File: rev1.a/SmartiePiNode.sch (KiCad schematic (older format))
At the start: 57 parts, among them CN1 USBMICROb, CN2 SWD, CN3 SX1238_TRX_HEADER, CN4 VIN, SW1 SW_PUSH, U1 ISL91127IR, U2 STM32L052_LQFP48, X1 abm10, X2 ABS25-32.768KHZ-6-T

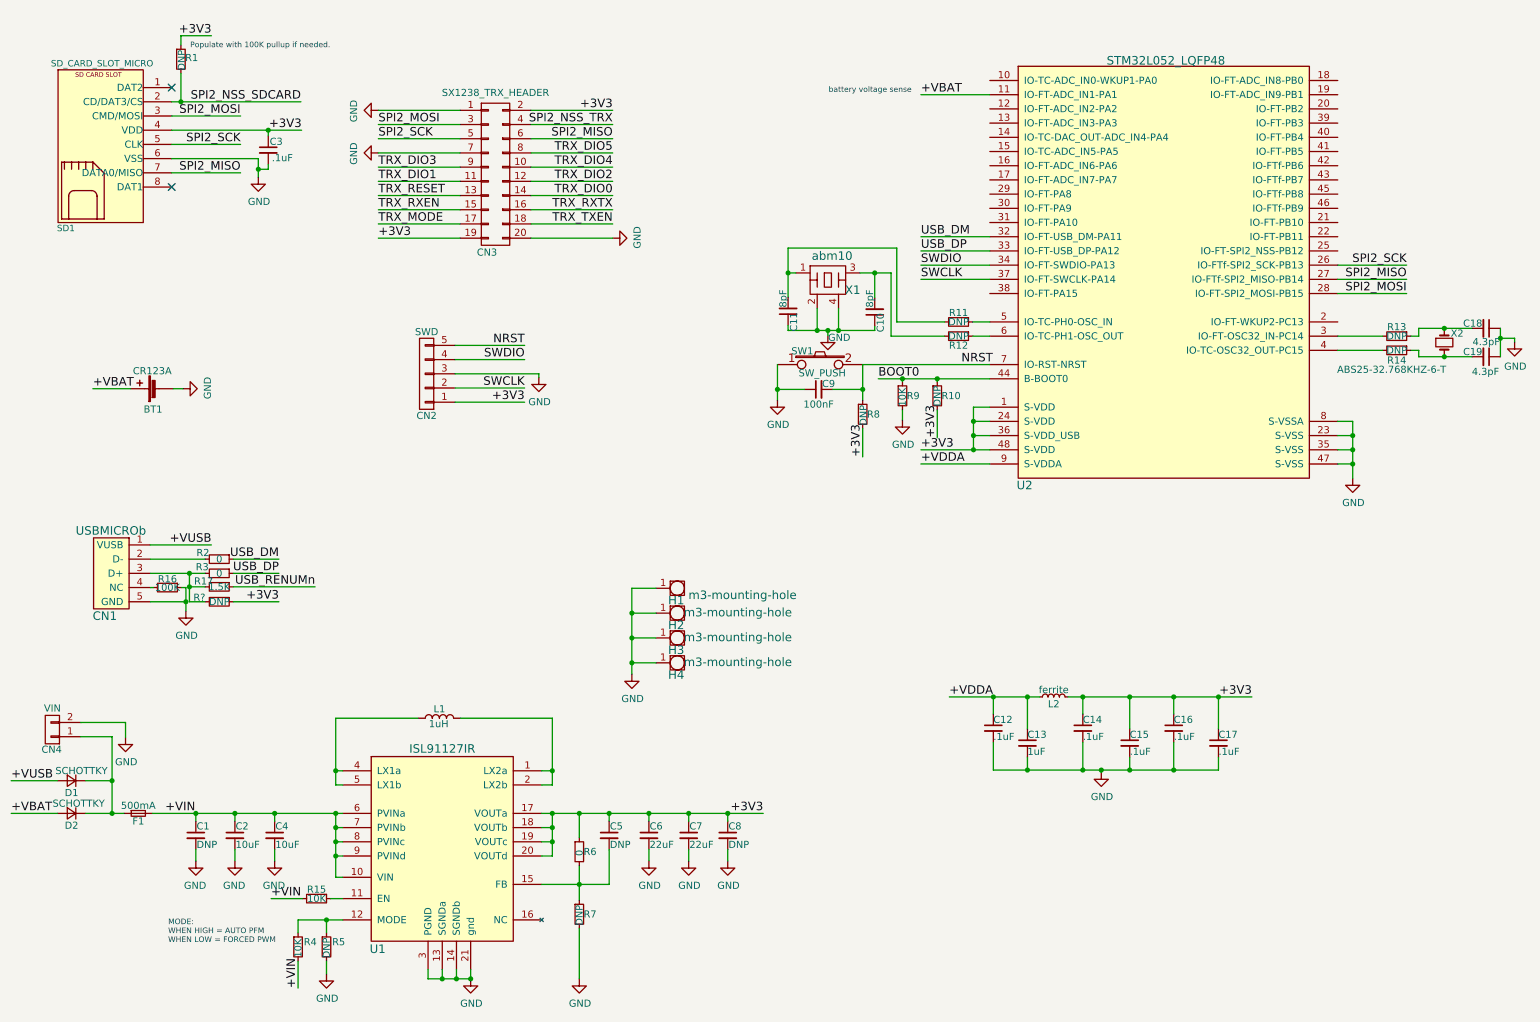
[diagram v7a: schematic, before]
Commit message: added battery sensing circuit and a bit more work on usb.
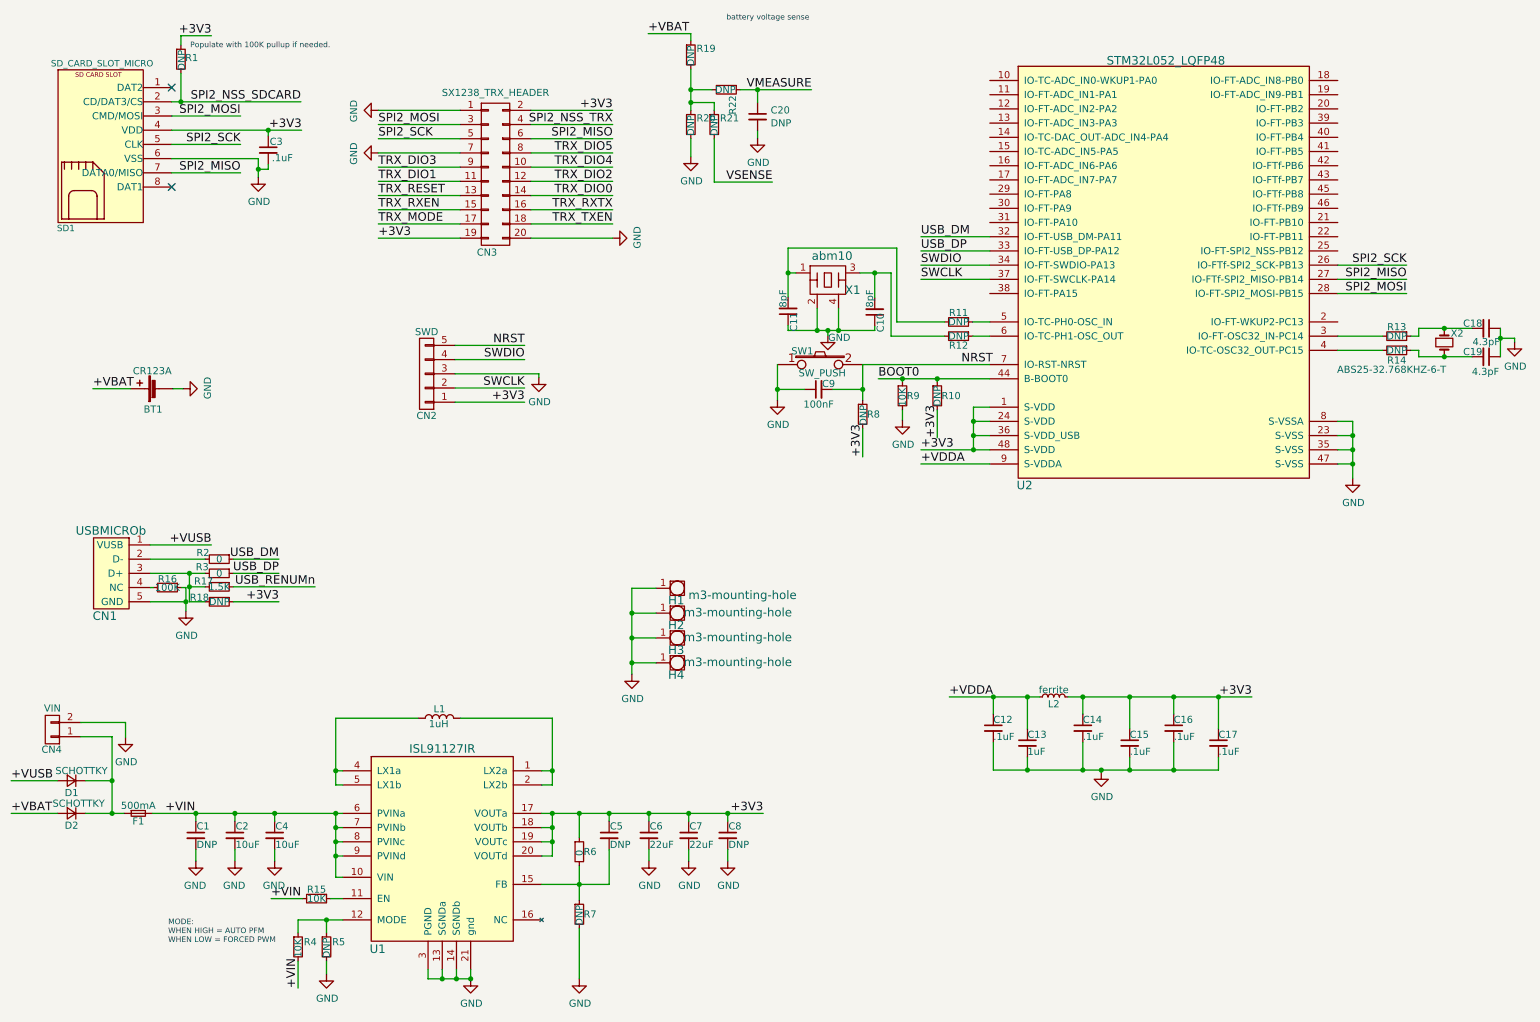
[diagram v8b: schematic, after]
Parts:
- added C20: DNP, Capacitors_SMD:C_0603, symbol C_Small
- added R19, R20, R21, R22: DNP, Resistors_SMD:R_0603, symbol R_Small
- R18: renamed from R?; footprint (none) -> Resistors_SMD:R_0603
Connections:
- net +VBAT: now also R19.1; no longer U2.11 (IO-FT-ADC_IN1-PA1)
- net GND: now also C20.2, R20.2
- new net: R19.2, R20.1, R21.1, R22.2
- new net VMEASURE: C20.1, R22.1
- new net VSENSE: R21.2
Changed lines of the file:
@@
 $EndComp
 $Comp
-L GND #PWR01
+L GND #PWR11
 U 1 1 5B041A53
 P 3720 7315
-F 0 "#PWR01" H 3720 7065 50  0001 C CNN
+F 0 "#PWR11" H 3720 7065 50  0001 C CNN
 F 1 "GND" H 3725 7142 50  0000 C CNN
 F 2 "" H 3720 7315 50  0001 C CNN
@@
 $EndComp
 $Comp
-L GND #PWR02
+L GND #PWR16
 U 1 1 5B041F18
 P 4975 6485
-F 0 "#PWR02" H 4975 6235 50  0001 C CNN
+F 0 "#PWR16" H 4975 6235 50  0001 C CNN
 F 1 "GND" H 4980 6312 50  0000 C CNN
 F 2 "" H 4975 6485 50  0001 C CNN
@@
 $EndComp
 $Comp
-L GND #PWR03
+L GND #PWR17
 U 1 1 5B04234F
 P 5255 6485
-F 0 "#PWR03" H 5255 6235 50  0001 C CNN
+F 0 "#PWR17" H 5255 6235 50  0001 C CNN
 F 1 "GND" H 5260 6312 50  0000 C CNN
 F 2 "" H 5255 6485 50  0001 C CNN
@@
 $EndComp
 $Comp
-L GND #PWR04
+L GND #PWR19
 U 1 1 5B0423C8
 P 5530 6485
-F 0 "#PWR04" H 5530 6235 50  0001 C CNN
+F 0 "#PWR19" H 5530 6235 50  0001 C CNN
 F 1 "GND" H 5535 6312 50  0000 C CNN
 F 2 "" H 5530 6485 50  0001 C CNN
@@
 $EndComp
 $Comp
-L GND #PWR05
+L GND #PWR7
 U 1 1 5B04306E
 P 2340 6485
-F 0 "#PWR05" H 2340 6235 50  0001 C CNN
+F 0 "#PWR7" H 2340 6235 50  0001 C CNN
 F 1 "GND" H 2345 6312 50  0000 C CNN
 F 2 "" H 2340 6485 50  0001 C CNN
@@
 $EndComp
 $Comp
-L GND #PWR06
+L GND #PWR5
 U 1 1 5B04307C
 P 2060 6485
-F 0 "#PWR06" H 2060 6235 50  0001 C CNN
+F 0 "#PWR5" H 2060 6235 50  0001 C CNN
 F 1 "GND" H 2065 6312 50  0000 C CNN
 F 2 "" H 2060 6485 50  0001 C CNN
@@
 $EndComp
 $Comp
-L GND #PWR07
+L GND #PWR4
 U 1 1 5B04308A
 P 1785 6485
-F 0 "#PWR07" H 1785 6235 50  0001 C CNN
+F 0 "#PWR4" H 1785 6235 50  0001 C CNN
 F 1 "GND" H 1790 6312 50  0000 C CNN
 F 2 "" H 1785 6485 50  0001 C CNN
@@
 $EndComp
 $Comp
-L GND #PWR08
+L GND #PWR8
 U 1 1 5B043F5D
 P 2705 7280
-F 0 "#PWR08" H 2705 7030 50  0001 C CNN
+F 0 "#PWR8" H 2705 7030 50  0001 C CNN
 F 1 "GND" H 2710 7107 50  0000 C CNN
 F 2 "" H 2705 7280 50  0001 C CNN
@@
 $EndComp
 $Comp
-L GND #PWR09
+L GND #PWR13
 U 1 1 5B044D4C
 P 4485 7315
-F 0 "#PWR09" H 4485 7065 50  0001 C CNN
+F 0 "#PWR13" H 4485 7065 50  0001 C CNN
 F 1 "GND" H 4490 7142 50  0000 C CNN
 F 2 "" H 4485 7315 50  0001 C CNN
@@
 $EndComp
 $Comp
-L GND #PWR010
+L GND #PWR25
 U 1 1 5B06F6EF
 P 9930 3790
-F 0 "#PWR010" H 9930 3540 50  0001 C CNN
+F 0 "#PWR25" H 9930 3540 50  0001 C CNN
 F 1 "GND" H 9935 3617 50  0000 C CNN
 F 2 "" H 9930 3790 50  0001 C CNN
@@
 $EndComp
 $Comp
-L GND #PWR011
+L GND #PWR23
 U 1 1 5B0753BB
 P 6760 3380
-F 0 "#PWR011" H 6760 3130 50  0001 C CNN
+F 0 "#PWR23" H 6760 3130 50  0001 C CNN
 F 1 "GND" H 6765 3207 50  0000 C CNN
 F 2 "" H 6760 3380 50  0001 C CNN
@@
 $EndComp
 $Comp
-L GND #PWR012
+L GND #PWR3
 U 1 1 5B081C3A
 P 1715 4725
-F 0 "#PWR012" H 1715 4475 50  0001 C CNN
+F 0 "#PWR3" H 1715 4475 50  0001 C CNN
 F 1 "GND" H 1720 4552 50  0000 C CNN
 F 2 "" H 1715 4725 50  0001 C CNN
@@
 $EndComp
 $Comp
-L GND #PWR013
+L GND #PWR21
 U 1 1 5B082DC4
 P 5880 3240
-F 0 "#PWR013" H 5880 2990 50  0001 C CNN
+F 0 "#PWR21" H 5880 2990 50  0001 C CNN
 F 1 "GND" H 5885 3067 50  0000 C CNN
 F 2 "" H 5880 3240 50  0001 C CNN
@@
 Connection ~ 10575 2935
 $Comp
-L GND #PWR014
+L GND #PWR26
 U 1 1 5B098D9A
 P 11070 2830
-F 0 "#PWR014" H 11070 2580 50  0001 C CNN
+F 0 "#PWR26" H 11070 2580 50  0001 C CNN
 F 1 "GND" H 11075 2657 50  0000 C CNN
 F 2 "" H 11070 2830 50  0001 C CNN
@@
 	2225 1540 2225 1670
 $Comp
-L GND #PWR015
+L GND #PWR6
 U 1 1 5B0A5E1E
 P 2225 1670
-F 0 "#PWR015" H 2225 1420 50  0001 C CNN
+F 0 "#PWR6" H 2225 1420 50  0001 C CNN
 F 1 "GND" H 2230 1497 50  0000 C CNN
 F 2 "" H 2225 1670 50  0001 C CNN
@@
 +3V3
 $Comp
-L GND #PWR016
+L GND #PWR9
 U 1 1 5B0AC996
 P 3070 1200
-F 0 "#PWR016" H 3070 950 50  0001 C CNN
+F 0 "#PWR9" H 3070 950 50  0001 C CNN
 F 1 "GND" H 3075 1027 50  0000 C CNN
 F 2 "" H 3070 1200 50  0001 C CNN
@@
 SPI2_SCK
 $Comp
-L GND #PWR017
+L GND #PWR10
 U 1 1 5B0AE690
 P 3070 1500
-F 0 "#PWR017" H 3070 1250 50  0001 C CNN
+F 0 "#PWR10" H 3070 1250 50  0001 C CNN
 F 1 "GND" H 3075 1327 50  0000 C CNN
 F 2 "" H 3070 1500 50  0001 C CNN
@@
 	4145 2100 4720 2100
 $Comp
-L GND #PWR018
+L GND #PWR14
 U 1 1 5B0AEB87
 P 4720 2100
-F 0 "#PWR018" H 4720 1850 50  0001 C CNN
+F 0 "#PWR14" H 4720 1850 50  0001 C CNN
 F 1 "GND" H 4725 1927 50  0000 C CNN
 F 2 "" H 4720 2100 50  0001 C CNN
@@
 	1625 3160 1695 3160
 $Comp
-L GND #PWR019
+L GND #PWR2
 U 1 1 5B0B10C1
 P 1695 3160
-F 0 "#PWR019" H 1695 2910 50  0001 C CNN
+F 0 "#PWR2" H 1695 2910 50  0001 C CNN
 F 1 "GND" H 1700 2987 50  0000 C CNN
 F 2 "" H 1695 3160 50  0001 C CNN
@@
 Wire Wire Line
 	810  5920 485  5920
-Wire Wire Line
-	6890 1090 7375 1090
-Text Label 6890 1090 0    60   ~ 0
+Text Label 4970 660  0    60   ~ 0
 +VBAT
-Text Notes 6240 1085 0    39   ~ 0
+Text Notes 5520 575  0    39   ~ 0
 battery voltage sense
 $Comp
@@
 NRST
 $Comp
-L GND #PWR020
+L GND #PWR12
 U 1 1 5B0B8F14
 P 4200 3080
-F 0 "#PWR020" H 4200 2830 50  0001 C CNN
+F 0 "#PWR12" H 4200 2830 50  0001 C CNN
 F 1 "GND" H 4205 2907 50  0000 C CNN
 F 2 "" H 4200 3080 50  0001 C CNN
@@
 $EndComp
 $Comp
-L GND #PWR021
+L GND #PWR24
 U 1 1 5B0C38AE
 P 8160 5860
-F 0 "#PWR021" H 8160 5610 50  0001 C CNN
+F 0 "#PWR24" H 8160 5610 50  0001 C CNN
 F 1 "GND" H 8165 5687 50  0000 C CNN
 F 2 "" H 8160 5860 50  0001 C CNN
@@
 Connection ~ 6235 2750
 $Comp
-L GND #PWR022
+L GND #PWR22
 U 1 1 5B1AE42D
 P 6235 2785
-F 0 "#PWR022" H 6235 2535 50  0001 C CNN
+F 0 "#PWR22" H 6235 2535 50  0001 C CNN
 F 1 "GND" H 6315 2770 50  0000 C CNN
 F 2 "" H 6235 2785 50  0001 C CNN
@@
 	4855 4565 4855 5170
 $Comp
-L GND #PWR023
+L GND #PWR15
 U 1 1 5B1D46F6
 P 4855 5170
-F 0 "#PWR023" H 4855 4920 50  0001 C CNN
+F 0 "#PWR15" H 4855 4920 50  0001 C CNN
 F 1 "GND" H 4860 4997 50  0000 C CNN
 F 2 "" H 4855 5170 50  0001 C CNN
@@
 	1290 5510 1290 5615
 $Comp
-L GND #PWR024
+L GND #PWR1
 U 1 1 5B2467F2
 P 1290 5615
-F 0 "#PWR024" H 1290 5365 50  0001 C CNN
+F 0 "#PWR1" H 1290 5365 50  0001 C CNN
 F 1 "GND" H 1295 5442 50  0000 C CNN
 F 2 "" H 1290 5615 50  0001 C CNN
@@
 Connection ~ 1740 4555
 $Comp
-L R_Small R?
+L R_Small R18
 U 1 1 5B272D51
 P 1950 4660
-F 0 "R?" V 1920 4520 50  0000 C CNN
+F 0 "R18" V 1920 4520 50  0000 C CNN
 F 1 "DNP" V 1950 4660 50  0000 C CNN
-F 2 "" H 1950 4660 50  0001 C CNN
+F 2 "Resistors_SMD:R_0603" H 1950 4660 50  0001 C CNN
 F 3 "" H 1950 4660 50  0001 C CNN
 	1    1950 4660
@@
 Text Label 2370 4660 2    60   ~ 0
 +3V3
+$Comp
+L R_Small R19
+U 1 1 5B27C6F8
+P 5270 810
+F 0 "R19" H 5310 855 50  0000 L CNN
+F 1 "DNP" V 5270 730 50  0000 L CNN
+F 2 "Resistors_SMD:R_0603" H 5270 810 50  0001 C CNN
+F 3 "" H 5270 810 50  0001 C CNN
+	1    5270 810
+	1    0    0    -1
+$EndComp
+$Comp
+L R_Small R20
+U 1 1 5B27CCB4
+P 5270 1300
+F 0 "R20" H 5310 1345 50  0000 L CNN
+F 1 "DNP" V 5270 1220 50  0000 L CNN
+F 2 "Resistors_SMD:R_0603" H 5270 1300 50  0001 C CNN
+F 3 "" H 5270 1300 50  0001 C CNN
+	1    5270 1300
+	1    0    0    -1
+$EndComp
+$Comp
+L R_Small R22
+U 1 1 5B27CF4F
+P 5520 1055
+F 0 "R22" H 5560 1100 50  0000 L CNN
+F 1 "DNP" V 5520 975 50  0000 L CNN
+F 2 "Resistors_SMD:R_0603" H 5520 1055 50  0001 C CNN
+F 3 "" H 5520 1055 50  0001 C CNN
+	1    5520 1055
+	0    1    1    0
+$EndComp
+$Comp
+L C_Small C20
+U 1 1 5B27D27D
+P 5740 1245
+F 0 "C20" H 5832 1291 50  0000 L CNN
+F 1 "DNP" H 5832 1200 50  0000 L CNN
+F 2 "Capacitors_SMD:C_0603" H 5740 1245 50  0001 C CNN
+F 3 "" H 5740 1245 50  0001 C CNN
+	1    5740 1245
+	1    0    0    -1
+$EndComp
+$Comp
+L R_Small R21
+U 1 1 5B27D74A
+P 5435 1300
+F 0 "R21" H 5475 1345 50  0000 L CNN
+F 1 "DNP" V 5435 1220 50  0000 L CNN
+F 2 "Resistors_SMD:R_0603" H 5435 1300 50  0001 C CNN
+F 3 "" H 5435 1300 50  0001 C CNN
+	1    5435 1300
+	1    0    0    -1
+$EndComp
+Wire Wire Line
+	5270 1400 5270 1525
+$Comp
+L GND #PWR18
+U 1 1 5B27DE3A
+P 5270 1525
+F 0 "#PWR18" H 5270 1275 50  0001 C CNN
+F 1 "GND" H 5275 1352 50  0000 C CNN
+F 2 "" H 5270 1525 50  0001 C CNN
+F 3 "" H 5270 1525 50  0001 C CNN
+	1    5270 1525
+	1    0    0    -1
+$EndComp
+Wire Wire Line
+	4970 660  5270 660
+Wire Wire Line
+	5270 660  5270 710
+Wire Wire Line
+	5270 910  5270 1200
+Wire Wire Line
+	5420 1055 5270 1055
+Connection ~ 5270 1055
+Wire Wire Line
+	5435 1200 5435 1145
+Wire Wire Line
+	5435 1145 5270 1145
+Connection ~ 5270 1145
+Wire Wire Line
+	5620 1055 6120 1055
+Wire Wire Line
+	5740 1145 5740 1055
+Connection ~ 5740 1055
+Wire Wire Line
+	5740 1345 5740 1395
+$Comp
+L GND #PWR20
+U 1 1 5B2802E4
+P 5740 1395
+F 0 "#PWR20" H 5740 1145 50  0001 C CNN
+F 1 "GND" H 5745 1222 50  0000 C CNN
+F 2 "" H 5740 1395 50  0001 C CNN
+F 3 "" H 5740 1395 50  0001 C CNN
+	1    5740 1395
+	1    0    0    -1
+$EndComp
+Wire Wire Line
+	5435 1400 5435 1705
+Text Label 6120 1055 2    60   ~ 0
+VMEASURE
+Text Label 5845 1705 2    60   ~ 0
+VSENSE
+Wire Wire Line
+	5435 1705 5845 1705
 $EndSCHEMATC
